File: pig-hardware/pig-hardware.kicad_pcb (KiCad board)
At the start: 2 copper layers, 65 x 56.5 mm, 33 parts, among them P1 PiB+_IO, P10 CONN_01X04, P2 CONN_01X04, P3 CONN_01X04, P4 CONN_01X02, P5 CONN_01X04, P6 CONN_01X08, P7 CONN_01X01, P8 CONN_01X02, P9 nrf24L01+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

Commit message: some more work in progress
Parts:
- added G***: LOGO, MyFootprints:pig_scale, F.Cu at (116.4, 96.6)
- added G***: LOGO, MyFootprints:topHat_scale, F.Cu at (116.6, 103.1)
- added G***: LOGO, MyFootprints:shutter_scale, B.Cu at (116.3, 96.2)
- added G***: LOGO, MyFootprints:nodeNumber_scale, F.Cu at (116.5, 89.5)
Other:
- board text added: "node:"
- board text added: "shutterKurt"

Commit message: removed pro & rfm from pcb
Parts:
- removed P10: CONN_01X04, Pin_Headers:Pin_Header_Straight_1x04
- removed P7: CONN_01X01, Pin_Headers:Pin_Header_Straight_1x01
- removed U1: ArduinoProMini-3v3, MyFootprints:Sparkfun-ArduinoProMini
- removed U3: RFM69HW, MyFootprints:RFM69
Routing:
- net 3V3: track 161.2 -> 80.4 mm, vias 1 -> 0
- net /PROMOSI: track 76.2 -> 0.05 mm, vias 1 -> 0
- net /PROMISO: track 75.3 -> 0.00 mm, vias 1 -> 0
- net /PROSCK: track 75.4 -> 0.13 mm, vias 1 -> 0
- net /NRFCSN: track 59.9 -> 0.89 mm, vias 2 -> 0
- net /NRFCE: track 56.9 -> 0.00 mm, vias 1 -> 0
- net NRFIRQ: track 56.1 -> 0.00 mm, vias 1 -> 0
- net ONEWIRE: track 83.0 -> 30.2 mm, vias 1 -> 0
- net RFMIRQ: track 38.1 -> 0.00 mm, vias 2 -> 0
- net OOKDAT: track 37.4 -> 0.00 mm
- net ATEMP: track 41.2 -> 8.23 mm
- net LED: track 30.4 -> 0.00 mm, vias 2 -> 0
- net SCL: track 34.2 -> 5.65 mm
- net SDA: track 34.1 -> 5.60 mm
- net GND: track 111.3 -> 83.3 mm, vias 7 -> 3
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- removed copper zone on F.Cu, net +5V

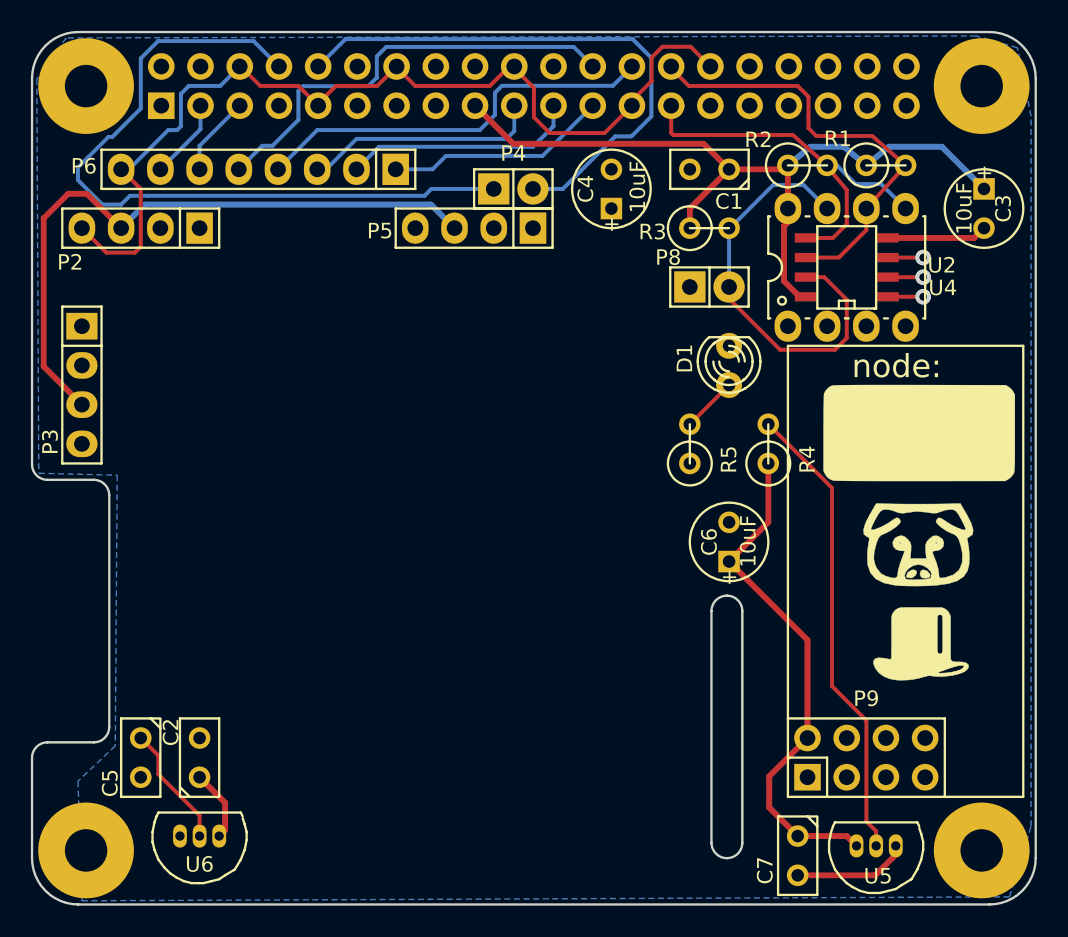
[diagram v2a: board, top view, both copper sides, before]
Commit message: update pcb for moteino
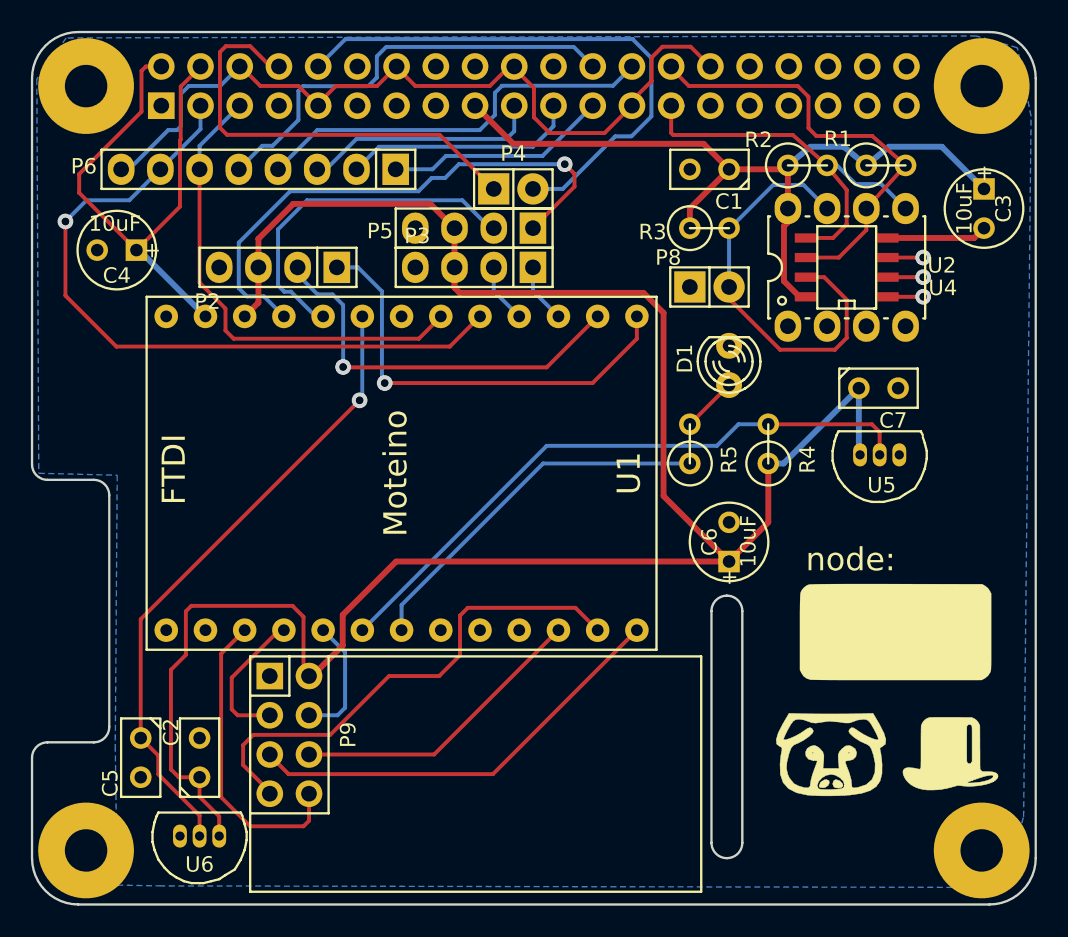
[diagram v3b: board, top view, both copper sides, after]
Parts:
- added U1: Moteino, MyFootprints:Moteino, F.Cu at (82.9, 92.1)
- moved P9 37.4 mm to (75.7, 109.0), turned to 270 degrees
- moved C4 32.3 mm to (64.5, 77.6), turned to 180 degrees
- moved C7 30.7 mm to (113.8, 86.6), turned to 0 degrees
- moved P3 26.5 mm to (87.6, 78.7), turned to 180 degrees
- moved U5 25.3 mm to (113.9, 90.9)
- moved G*** 14.7 mm to (110.7, 110.2)
- moved G*** 13.0 mm to (114.9, 102.4)
- moved P2 9.25 mm to (74.9, 78.7)
- moved G*** 7.36 mm to (118.5, 110.2)
- moved G*** 4.93 mm to (115.1, 101.0)
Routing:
- net 3V3: track 80.4 -> 135.8 mm
- net SDA: track 5.60 -> 47.0 mm, vias 0 -> 1
- net +5V: track 0.00 -> 37.2 mm
- net /PROTX: track 0.00 -> 35.4 mm, vias 0 -> 1
- net ATEMP: track 8.23 -> 41.5 mm, vias 0 -> 1
- net /PROMISO: track 0.00 -> 32.7 mm
- net /SWTX1: track 0.00 -> 28.5 mm, vias 0 -> 1
- net /PROSCK: track 0.13 -> 28.2 mm
- net /SWRX1: track 0.00 -> 26.1 mm, vias 0 -> 1
- net SCL: track 5.65 -> 31.6 mm
- net LED: track 0.00 -> 24.1 mm
- net /PRORX: track 0.00 -> 22.9 mm
- net NRFIRQ: track 0.00 -> 19.8 mm
- net /PROMOSI: track 0.05 -> 19.5 mm
- net PITX: track 47.8 -> 28.8 mm
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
